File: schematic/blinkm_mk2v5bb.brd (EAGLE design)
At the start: 17 x 17.7 mm, 20 parts, among them CN1 1X4SMT, J1 usb, Q1 MOSFET-PCHANNEL, U1 Tiny85-20-SMT

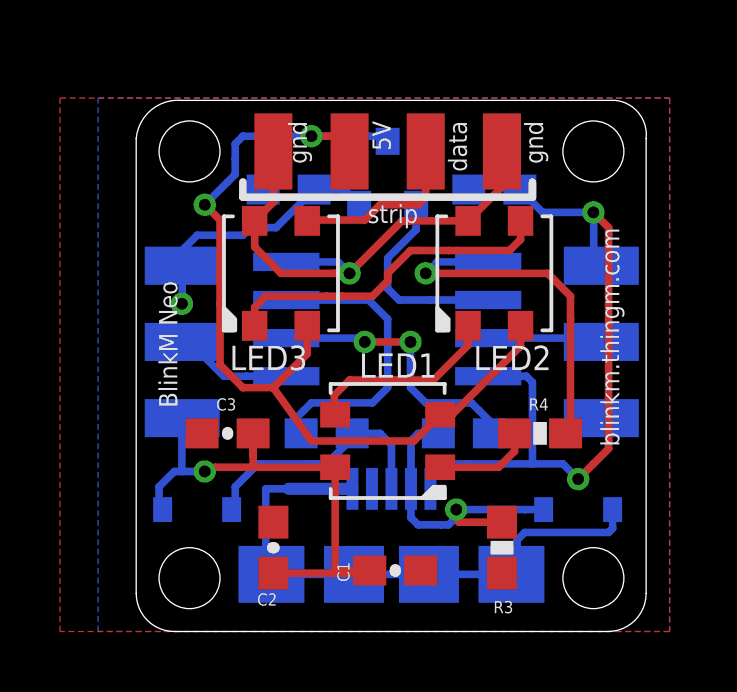
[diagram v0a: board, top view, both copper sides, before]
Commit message: added _3535aa,ab ideas
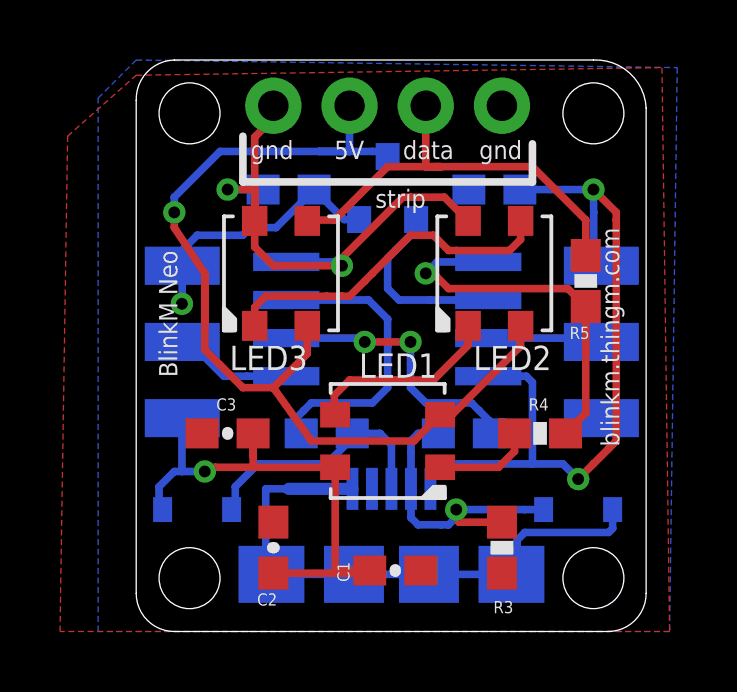
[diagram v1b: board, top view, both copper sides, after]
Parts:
- removed CN1: 1X4SMT, adafruit:1X4-SMT
- added J2: strip, SparkFun-Connectors:1X04_NO_SILK_ALL_ROUND
- added R5: nonpop, SparkFun-Passives:0603-RES
- moved Q1 0.51 mm to (8.38, 14.7)
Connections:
- net GND: now also J2.1, J2.4; no longer CN1.1, CN1.4
- net LEDDAT: now also R5.1
- net LEDDO: now also J2.3, R5.2; no longer CN1.3
- net VDD: now also J2.2; no longer CN1.2
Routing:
- net LEDDO: track 5.80 -> 14.7 mm
- net VDD: track 32.9 -> 34.6 mm, vias 2 -> 1
- net 5V: track 33.5 -> 35.1 mm
- net GND: track 56.5 -> 58.1 mm, vias 2 -> 3
- net LEDDAT: track 12.0 -> 12.7 mm
- net LEDCTL: track 6.71 -> 6.21 mm
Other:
- board size 17 x 17.7 mm -> 17 x 19.1 mm
- board text added: "+"
- board text added: "-"
- board text added: "blinkm_mk2v5bb"
- board text added: "dat"
- board text removed: "blinkm_mk2v5a"
